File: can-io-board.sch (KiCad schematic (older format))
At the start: 21 parts, among them J1 CONN_IO, J2 CONN_PWM, U1 STM32F302K8U6, U2 MCP1703, U3 MAX3051, X1 16MHz 10ppm

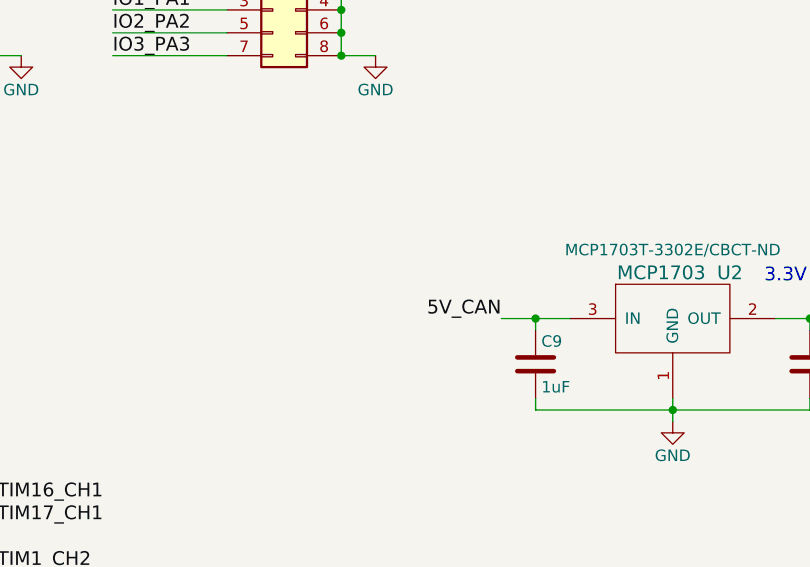
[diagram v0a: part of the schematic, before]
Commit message: Add CAN reverse voltage protection diode
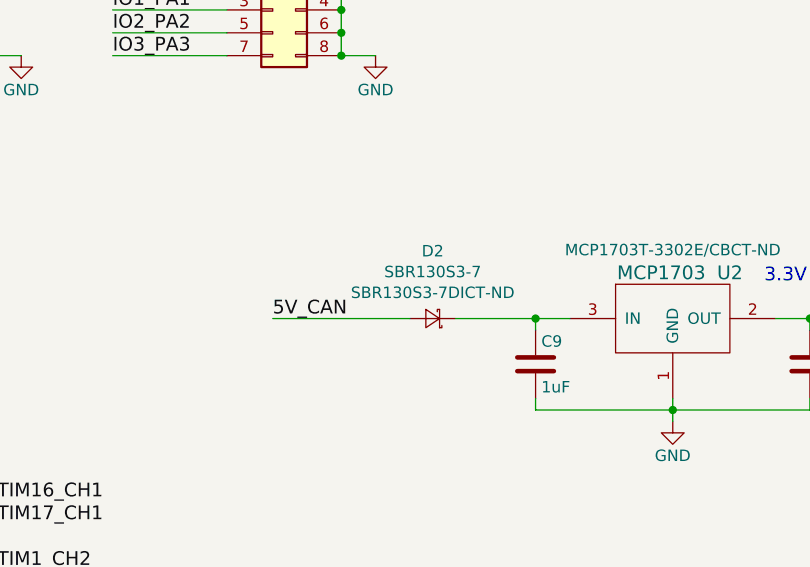
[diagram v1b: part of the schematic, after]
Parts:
- added D2: SBR130S3-7, Diode_SMD:D_SOD-323_HandSoldering, symbol Device:D_Schottky_Small
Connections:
- net 5V_CAN: now also D2.2 (A); no longer C9.1, U2.3 (IN)
- new net: C9.1, D2.1 (K), U2.3 (IN)
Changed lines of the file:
@@
 	1    0    0    -1
 $EndComp
-Text Label 8150 2900 2    60   ~ 0
+Text Label 7150 2900 0    60   ~ 0
 5V_CAN
 $Comp
@@
 	8300 2900 8300 2950
 Wire Wire Line
-	8150 2900 8300 2900
+	7950 2900 8300 2900
 Wire Wire Line
 	9500 2900 9500 2950
@@
 Wire Wire Line
 	8000 5150 8100 5150
+$Comp
+L Device:D_Schottky_Small D2
+U 1 1 5BD6F803
+P 7850 2900
+F 0 "D2" H 7850 2605 50  0000 C CNN
+F 1 "SBR130S3-7" H 7850 2696 50  0000 C CNN
+F 2 "Diode_SMD:D_SOD-323_HandSoldering" V 7850 2900 50  0001 C CNN
+F 3 "~" V 7850 2900 50  0001 C CNN
+F 4 "SBR130S3-7DICT-ND" H 7850 2787 50  0000 C CNN "Digikey"
+	1    7850 2900
+	-1   0    0    1
+$EndComp
+Wire Wire Line
+	7150 2900 7750 2900
 $EndSCHEMATC
